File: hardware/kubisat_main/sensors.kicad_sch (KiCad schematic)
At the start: 0 parts

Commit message: added arduino code, more items on main schematic
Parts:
- added C10: 1u, Capacitor_SMD:C_0805_2012Metric, symbol Device:C
- added C3, C6, C9: 100n, Capacitor_SMD:C_0805_2012Metric, symbol Device:C
- added C4: 10n, Capacitor_SMD:C_0805_2012Metric, symbol Device:C
- added C5: 2n2, Capacitor_SMD:C_0805_2012Metric, symbol Device:C
- added C7: 4u7, Capacitor_SMD:C_0805_2012Metric, symbol Device:C
- added C8: 200n, Capacitor_SMD:C_0805_2012Metric, symbol Device:C
- added R3, R4, R5: 4k7, Resistor_SMD:R_0805_2012Metric, symbol Device:R
- added R6, R7, R8, R9: 10k, Resistor_SMD:R_0805_2012Metric, symbol Device:R
- added U3: MPU-6050, Sensor_Motion:InvenSense_QFN-24_4x4mm_P0.5mm, symbol Sensor_Motion:MPU-6050
- added U4: MMC5883MA, Package_LGA:LGA-16_3x3mm_P0.5mm, symbol Sensor_Magnetic:MMC5883MA
- added U5: BMP280, Package_LGA:Bosch_LGA-8_2x2.5mm_P0.65mm_ClockwisePinNumbering, symbol Sensor_Pressure:BMP280
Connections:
- new net: R8.1, U5.5 (SDO)
- new net: R9.1, U5.2 (CSB)
- new net: U3.7 (AUX_CL), U4.1 (SCL)
- new net: C7.1, U4.10 (CAP)
- new net: C8.2, U4.12 (SETC)
- new net: U3.6 (AUX_DA), U4.16 (SDA)
- new net: C8.1, U4.8 (SETP)
- new net: C3.2, U3.10 (REGOUT)
- new net: C5.1, U3.20 (CPOUT)
- new net: R5.2, U3.9 (AD0)
- new net +3V3: C10.1, C4.1, C6.1, C9.1, R3.2, R4.1, R6.2, R7.2, R8.2, R9.2, U3.13 (VDD), U3.8 (VLOGIC), U4.13 (VDDIO), U4.2 (VDD), U4.4 (S1), U5.6 (VDDIO), U5.8 (VDD)
- new net GND: C10.2, C3.1, C4.2, C5.2, C6.2, C7.2, C9.2, R5.1, U3.1 (CLKIN), U3.11 (FSYNC), U3.18 (GND), U4.11 (GND), U4.9 (GND), U5.1 (GND), U5.7 (GND)
- new net MDRDY: U4.15 (INT)
- new net SCL: R4.2, R6.1, U3.23 (SCL), U5.4 (SCK)
- new net SDA: R3.1, R7.1, U3.24 (SDA), U5.3 (SDI)
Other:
- note added: "9DOF MPU6050 + HMC5883L"
- note added: "BMP280 I2C MODE"

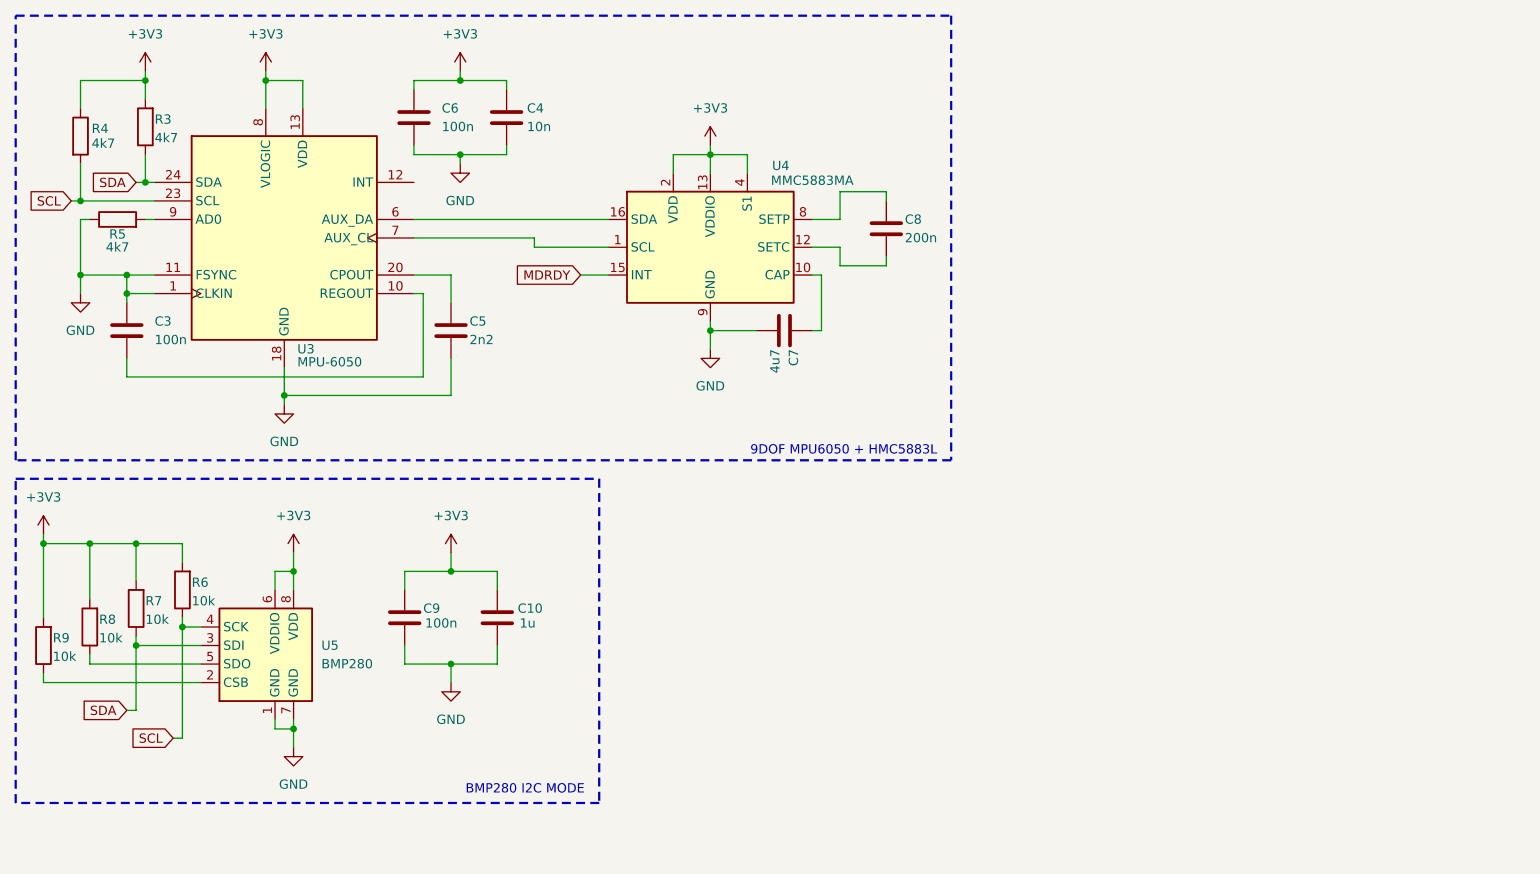
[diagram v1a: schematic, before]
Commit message: added elements and traces to main pcb
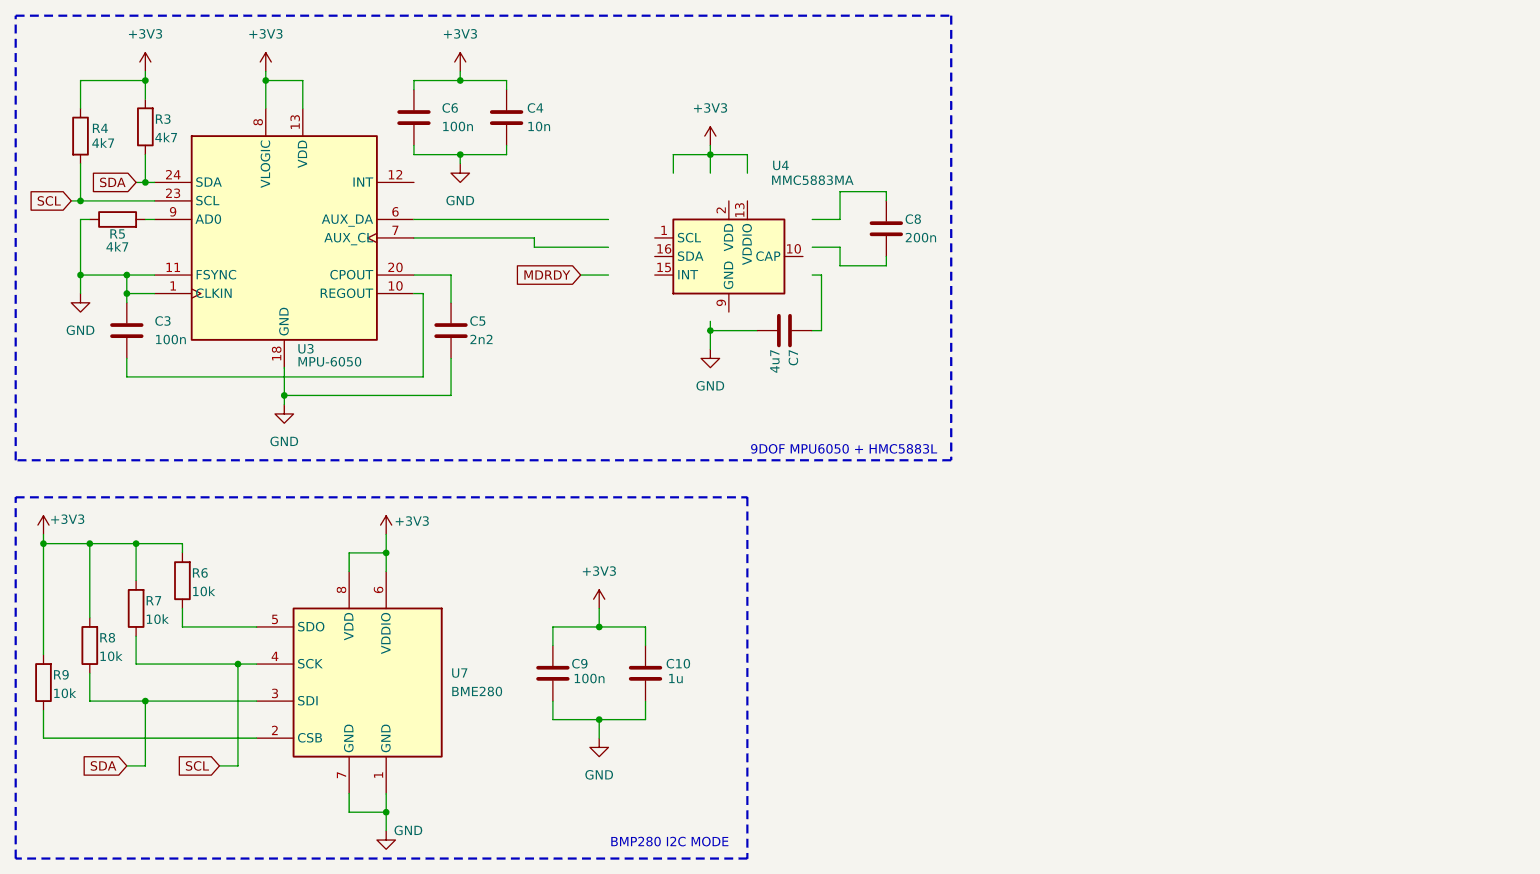
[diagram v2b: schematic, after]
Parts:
- removed U5: BMP280, Package_LGA:Bosch_LGA-8_2x2.5mm_P0.65mm_ClockwisePinNumbering, symbol Sensor_Pressure:BMP280
- added U7: BME280, Package_LGA:Bosch_LGA-8_2.5x2.5mm_P0.65mm_ClockwisePinNumbering, symbol Sensor:BME280
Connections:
- net +3V3: now also U7.6 (VDDIO), U7.8 (VDD); no longer U4.13 (VDDIO), U4.2 (VDD), U4.4 (S1)
- net GND: now also U7.1 (GND), U7.7 (GND); no longer U4.11 (GND), U4.9 (GND)
- net MDRDY: no longer U4.15 (INT)
- net SCL: now also R7.1, U7.4 (SCK); no longer R6.1
- net SDA: now also R8.1, U7.3 (SDI); no longer R7.1
- net at R9.1: now also U7.2 (CSB)
- net at U4.1 (SCL): no longer U3.7 (AUX_CL)
- net at U4.10 (CAP): no longer C7.1
- net at U4.12 (NC): no longer C8.2
- net at U4.16 (SDA): no longer U3.6 (AUX_DA)
- net at U4.8 (NC): no longer C8.1
- new net: U4.11 (GND), U4.9 (GND)
- new net: R6.1, U7.5 (SDO)
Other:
- moved on the sheet: C10, C9, R6, R8, R9

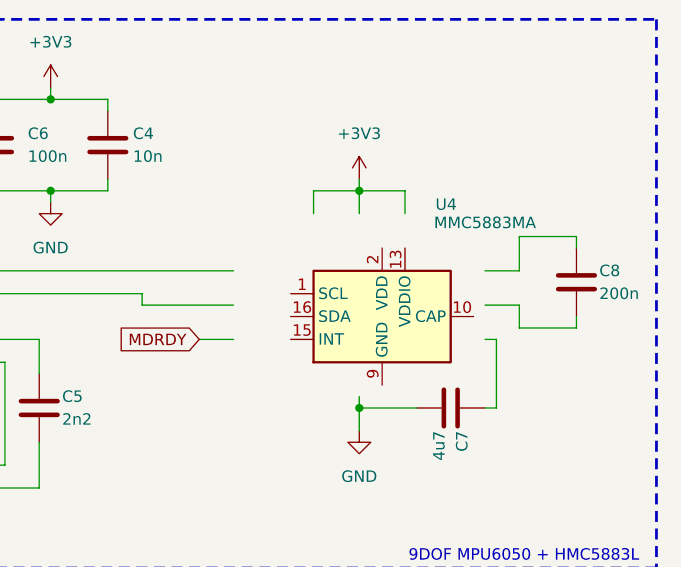
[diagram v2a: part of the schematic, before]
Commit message: added microsd footprint
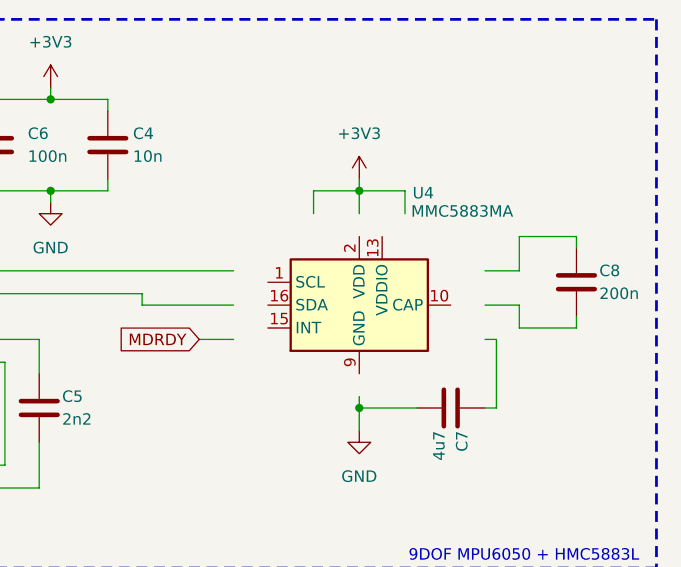
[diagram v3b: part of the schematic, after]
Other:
- moved on the sheet: U4
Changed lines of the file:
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@@
 	(symbol
 		(lib_id "Sensor_Magnetic:MMC5883MA")
-		(at 111.76 46.99 0)
+		(at 109.22 45.72 0)
 		(unit 1)
 		(exclude_from_sim no)
@@
 		(fields_autoplaced yes)
 		(property "Reference" "U4"
-			(at 118.872 34.544 0)
+			(at 116.332 33.274 0)
 			(effects
 				(font
@@
 		)
 		(property "Value" "MMC5883MA"
-			(at 123.19 36.576 0)
+			(at 120.65 35.306 0)
 			(effects
 				(font
@@
 		)
 		(property "Footprint" "Package_LGA:LGA-16_3x3mm_P0.5mm"
-			(at 111.76 64.77 0)
+			(at 109.22 63.5 0)
 			(effects
 				(font
@@
 		)
 		(property "Datasheet" "http://www.memsic.com/userfiles/files/DataSheets/Magnetic-Sensors-Datasheets/MMC5883MA-RevC.pdf"
-			(at 113.03 21.844 0)
+			(at 110.49 20.574 0)
 			(effects
 				(font
@@
 		)
 		(property "Description" "3-axis Magnetic Sensor, I2C Interface, LGA-16"
-			(at 111.506 24.13 0)
+			(at 108.966 22.86 0)
 			(effects
 				(font

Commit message: added elements to cpu schematic
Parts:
- added U8: DS3231M, Package_SO:SOIC-16W_7.5x10.3mm_P1.27mm, symbol Timer_RTC:DS3231M
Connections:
- new net: U8.10 (GND), U8.11 (GND), U8.12 (GND), U8.13 (GND), U8.5 (GND), U8.6 (GND), U8.7 (GND), U8.8 (GND), U8.9 (GND)
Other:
- moved on the sheet: C10, C9, R6, R7, R8, R9, U7

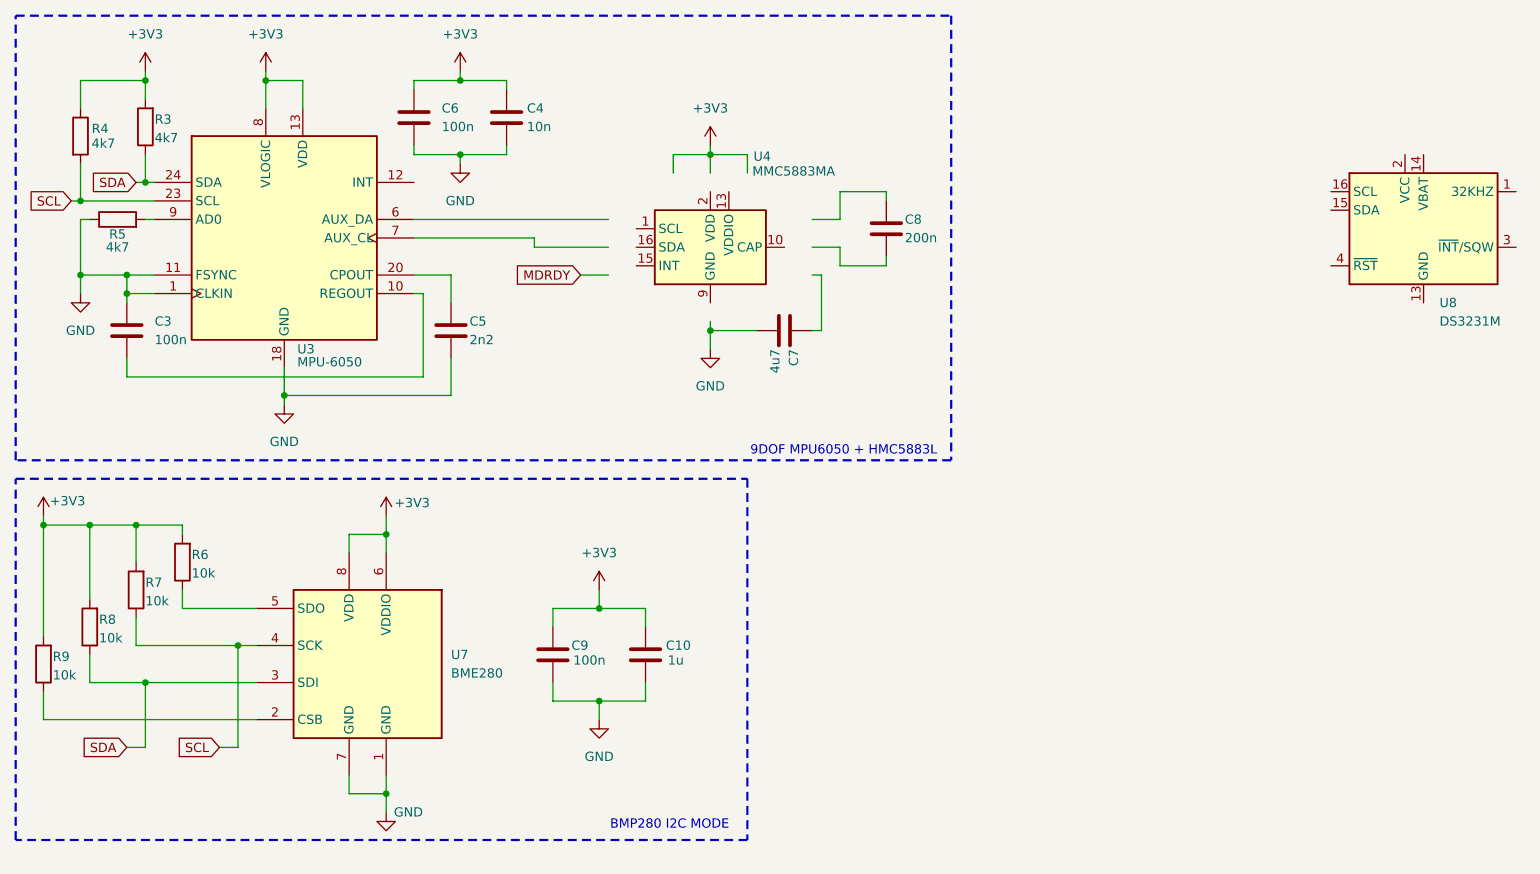
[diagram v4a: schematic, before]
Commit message: changed strucutre, split main into 2 sseparate boards
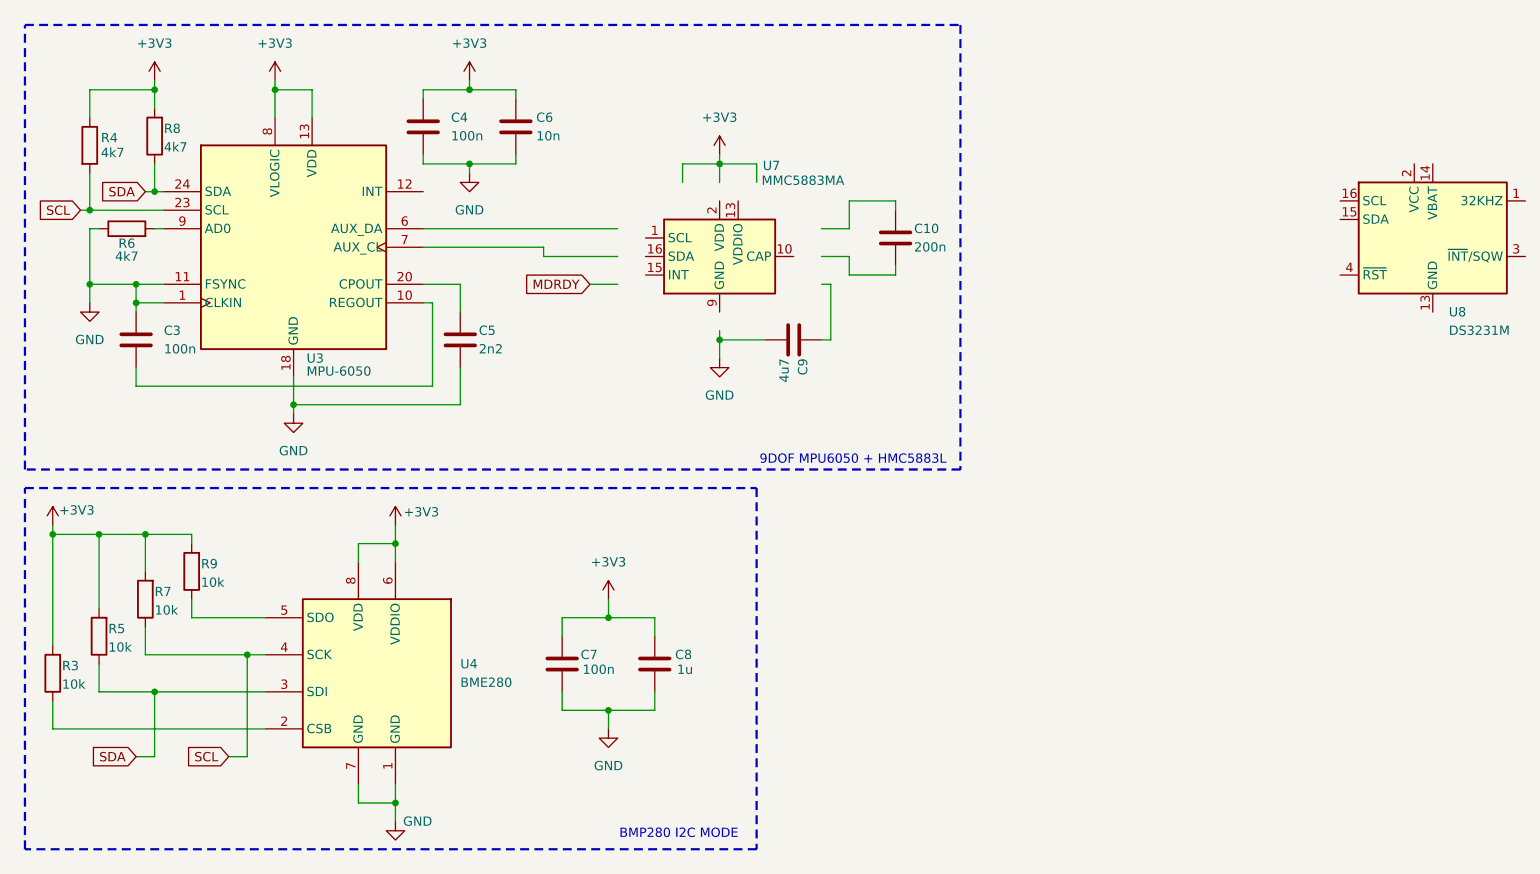
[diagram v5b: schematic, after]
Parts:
- removed U4: MMC5883MA, Package_LGA:LGA-16_3x3mm_P0.5mm, symbol Sensor_Magnetic:MMC5883MA
- removed U7: BME280, Package_LGA:Bosch_LGA-8_2.5x2.5mm_P0.65mm_ClockwisePinNumbering, symbol Sensor:BME280
- added U4: BME280, Package_LGA:Bosch_LGA-8_2.5x2.5mm_P0.65mm_ClockwisePinNumbering, symbol Sensor:BME280
- added U7: MMC5883MA, Package_LGA:LGA-16_3x3mm_P0.5mm, symbol Sensor_Magnetic:MMC5883MA
- C10: value 1u -> 200n
- C4: value 10n -> 100n
- C6: value 100n -> 10n
- C7: value 4u7 -> 100n
- C8: value 200n -> 1u
- C9: value 100n -> 4u7
- R3, R5: value 4k7 -> 10k
- R6, R8: value 10k -> 4k7
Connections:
- net +3V3: now also C7.1, C8.1, R5.2, U4.6 (VDDIO), U4.8 (VDD); no longer C10.1, C9.1, R6.2
- net GND: now also C8.2, R6.1, U4.1 (GND), U4.7 (GND); no longer C10.2, R5.1
- net SCL: now also U4.4 (SCK)
- net SDA: now also R5.1, U4.3 (SDI); no longer R3.1
- net at R9.1: now also U4.5 (SDO)
- net at U3.9 (AD0): now also R6.2; no longer R5.2
- new net: R3.1, U4.2 (CSB)
- new net: U7.11 (GND), U7.9 (GND)
